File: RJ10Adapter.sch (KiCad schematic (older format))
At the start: 11 parts, among them J1 RJ10, J2 Conn_01x06_Male, J3 USB_B_Micro, SW1 SW_Push, U1 AMS1117-3.3, U2 ESP-12F

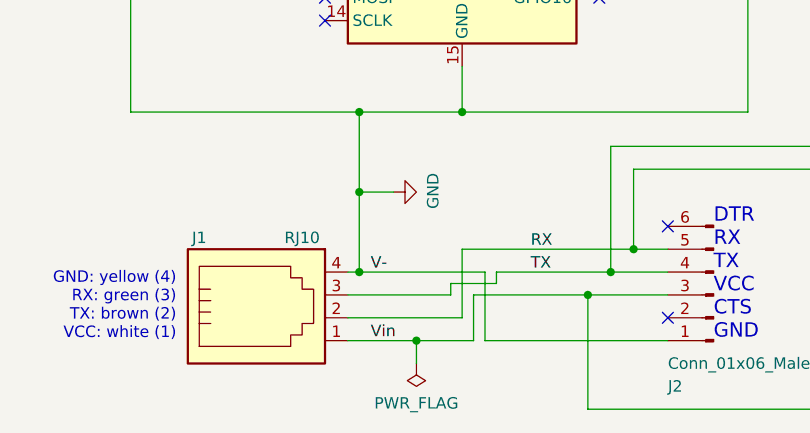
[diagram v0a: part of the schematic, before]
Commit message: Changed RX and TX
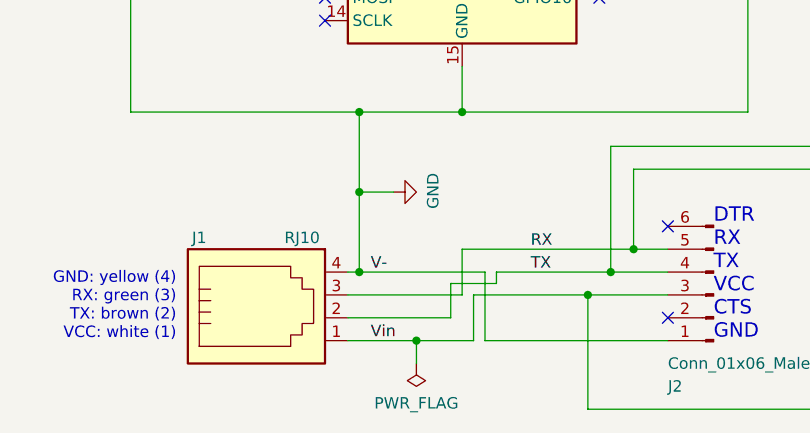
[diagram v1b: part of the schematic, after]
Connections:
- net RX: now also J1.3; no longer J1.2
- net TX: now also J1.2; no longer J1.3
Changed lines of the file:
@@
 Sheet 1 1
 Title "RJ FTDI Adapter"
-Date "2019-10-24"
-Rev "1.2"
+Date "2020-08-09"
+Rev "1.3"
 Comp "haus-automatisierung.com"
 Comment1 "Matthias Kleine"
@@
 	4050 3600 4100 3600
 Wire Wire Line
-	4050 3800 4550 3800
-Wire Wire Line
-	4550 3800 4550 3500
-Wire Wire Line
 	4550 3500 5300 3500
-Wire Wire Line
-	4050 3700 4500 3700
-Wire Wire Line
-	4500 3700 4500 3650
 Wire Wire Line
 	4500 3650 4700 3650
@@
 Wire Wire Line
 	5450 1600 5450 1150
+Wire Wire Line
+	4500 3800 4050 3800
+Wire Wire Line
+	4500 3650 4500 3800
+Wire Wire Line
+	4050 3700 4550 3700
+Wire Wire Line
+	4550 3700 4550 3500
 $EndSCHEMATC

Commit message: Readme and minor changes
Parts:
- J3: symbol Connector:USB_B_Micro -> RJ10Adapter-rescue:USB_B_Micro-Connector
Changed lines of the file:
@@
 EESchema Schematic File Version 4
-LIBS:RJ10Adapter-cache
 EELAYER 30 0
 EELAYER END
@@
 $EndComp
 $Comp
-L Connector:USB_B_Micro J3
+L RJ10Adapter-rescue:USB_B_Micro-Connector J3
 U 1 1 5CAF7777
 P 2050 1200
